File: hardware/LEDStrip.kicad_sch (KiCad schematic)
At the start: 3 parts, among them J501 WAGO 2065-100, J502 WAGO 2065-100, U501 74AHC1G125

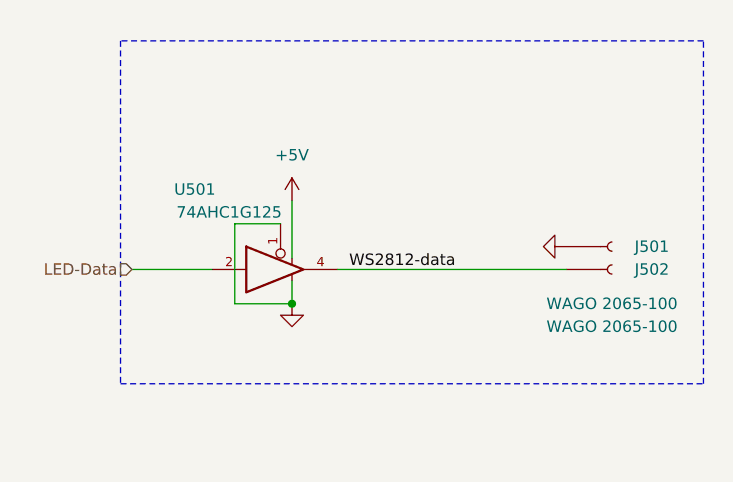
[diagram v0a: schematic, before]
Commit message: Update power routing
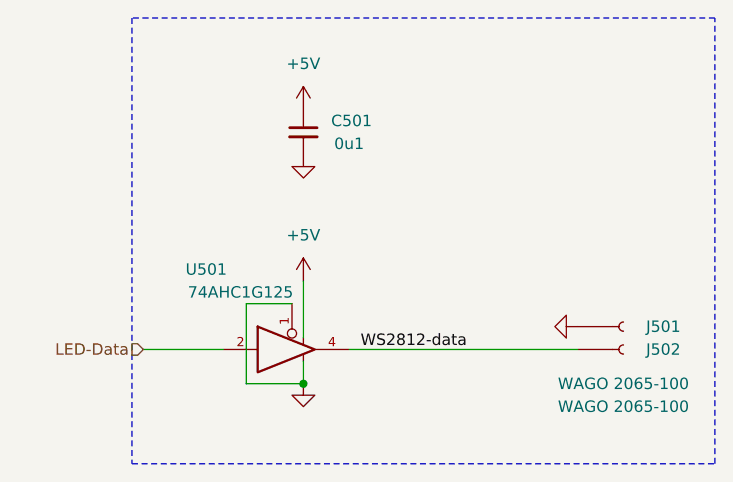
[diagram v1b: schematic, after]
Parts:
- added C501: 0u1, V2_Capacitor_SMD:C_1608, symbol V2_Capacitor:1608_0u1
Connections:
- net +5V: now also C501.1
- net GND: now also C501.2
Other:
- moved on the sheet: J501, J502, U501
